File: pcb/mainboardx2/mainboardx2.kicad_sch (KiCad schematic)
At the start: 28 parts, among them J1 Compass, J10 Right, J11 Back, J12 Conn_01x03_Socket, J13 Conn_01x03_Socket, J14 Conn_01x03_Socket, J15 Conn_01x03_Socket, J16 Conn_01x03_Socket, J17 Conn_01x03_Socket, J18 Conn_01x03_Socket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

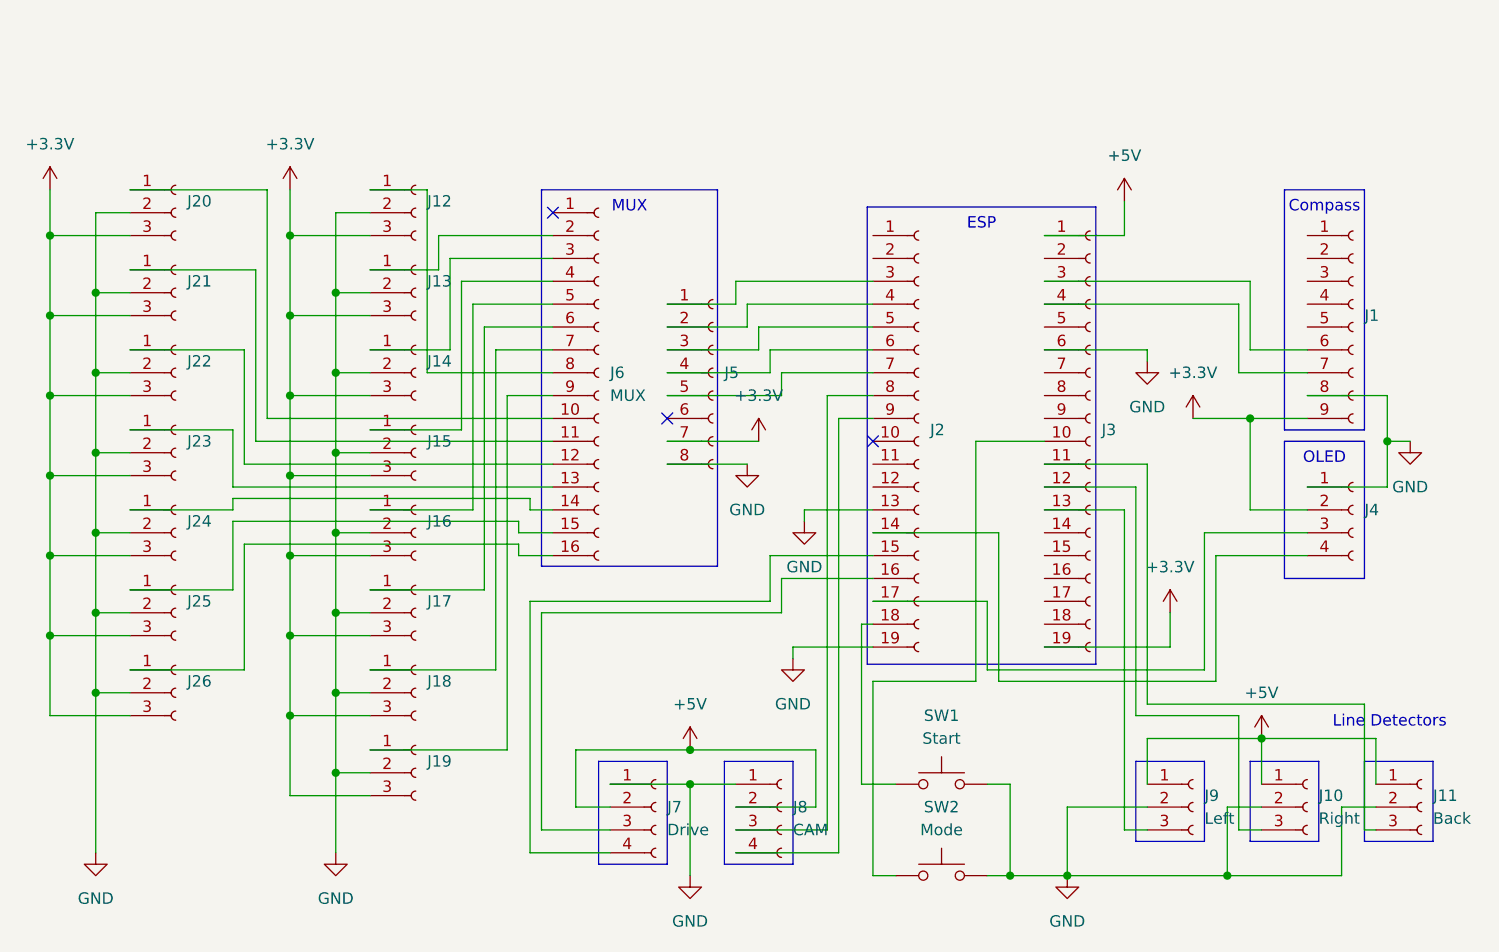
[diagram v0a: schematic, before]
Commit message: pins remapping
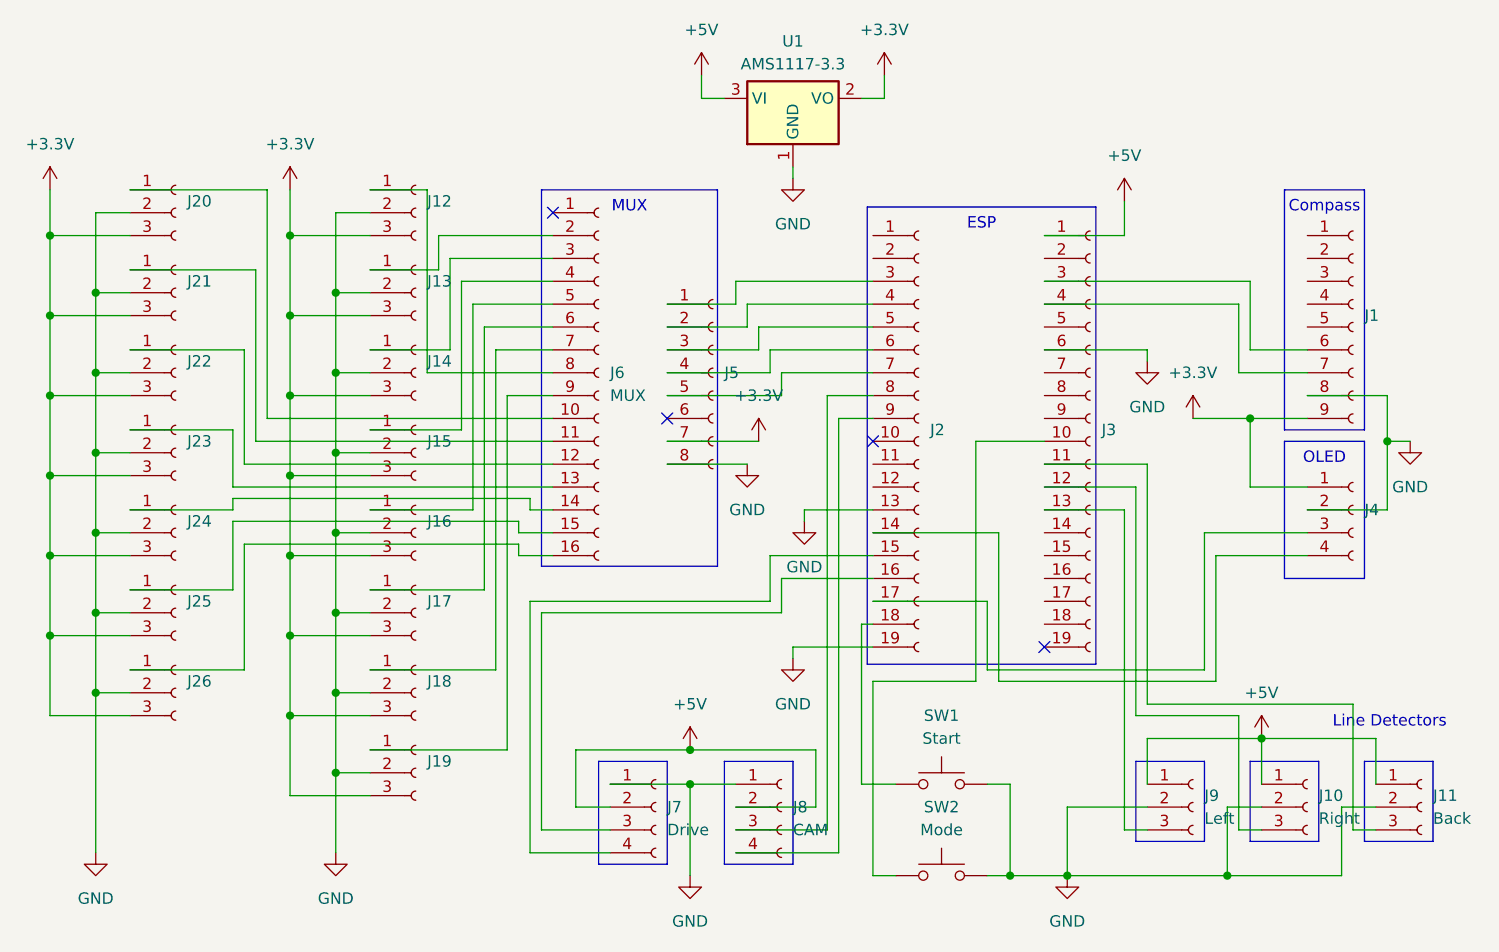
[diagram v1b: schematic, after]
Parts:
- added U1: AMS1117-3.3, Package_TO_SOT_SMD:SOT-223-3_TabPin2, symbol Regulator_Linear:AMS1117-3.3
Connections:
- net +3.3V: now also J4.1 (Pin_1), U1.2 (VO); no longer J3.19 (Pin_19), J4.2 (Pin_2)
- net +5V: now also U1.3 (VI)
- net GND: now also J4.2 (Pin_2), U1.1 (GND); no longer J4.1 (Pin_1)
- no-connect marks 3 -> 4

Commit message: calibration
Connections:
- net at J2.3 (Pin_3): no longer J5.1 (Pin_1)
- net at J3.5 (Pin_5): now also J5.1 (Pin_1)
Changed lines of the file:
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@@
 	(wire
 		(pts
-			(xy 73.66 54.61) (xy 69.85 54.61)
+			(xy 171.45 66.04) (xy 171.45 68.58)
 		)
 		(stroke
@@
 	(wire
 		(pts
-			(xy 38.1 57.15) (xy 38.1 66.04)
+			(xy 73.66 54.61) (xy 69.85 54.61)
 		)
 		(stroke
@@
 	(wire
 		(pts
-			(xy 46.99 83.82) (xy 38.1 83.82)
+			(xy 38.1 57.15) (xy 38.1 66.04)
 		)
 		(stroke
@@
 	(wire
 		(pts
-			(xy 73.66 105.41) (xy 88.9 105.41)
+			(xy 46.99 83.82) (xy 38.1 83.82)
 		)
 		(stroke
@@
 	(wire
 		(pts
-			(xy 114.3 53.34) (xy 129.54 53.34)
+			(xy 73.66 105.41) (xy 88.9 105.41)
 		)
 		(stroke
@@
 	(wire
 		(pts
+			(xy 125.73 53.34) (xy 125.73 43.18)
+		)
+		(stroke
+			(width 0)
+			(type default)
+		)
+	)
+	(wire
+		(pts
 			(xy 125.73 68.58) (xy 129.54 68.58)
 		)
@@
 	(wire
 		(pts
+			(xy 125.73 43.18) (xy 143.51 43.18)
+		)
+		(stroke
+			(width 0)
+			(type default)
+		)
+	)
+	(wire
+		(pts
 			(xy 90.17 80.01) (xy 90.17 81.28)
 		)
@@
 	(wire
 		(pts
+			(xy 114.3 53.34) (xy 125.73 53.34)
+		)
+		(stroke
+			(width 0)
+			(type default)
+		)
+	)
+	(wire
+		(pts
 			(xy 129.54 119.38) (xy 132.08 119.38)
 		)
@@
 	(wire
 		(pts
+			(xy 143.51 43.18) (xy 143.51 58.42)
+		)
+		(stroke
+			(width 0)
+			(type default)
+		)
+	)
+	(wire
+		(pts
 			(xy 73.66 66.04) (xy 64.77 66.04)
 		)
@@
 	(wire
 		(pts
-			(xy 148.59 60.96) (xy 160.02 60.96)
+			(xy 148.59 60.96) (xy 157.48 60.96)
 		)
 		(stroke
@@
 	(wire
 		(pts
-			(xy 160.02 60.96) (xy 160.02 62.23)
+			(xy 157.48 60.96) (xy 157.48 62.23)
 		)
 		(stroke
@@
 	(wire
 		(pts
-			(xy 165.1 68.58) (xy 171.45 68.58)
+			(xy 167.64 66.04) (xy 171.45 66.04)
 		)
 		(stroke
@@
 	(wire
 		(pts
+			(xy 143.51 58.42) (xy 148.59 58.42)
+		)
+		(stroke
+			(width 0)
+			(type default)
+		)
+	)
+	(wire
+		(pts
 			(xy 144.78 119.38) (xy 151.13 119.38)
 		)
@@
 	(symbol
 		(lib_id "power:+3.3V")
-		(at 165.1 68.58 0)
+		(at 167.64 66.04 0)
 		(unit 1)
 		(exclude_from_sim no)
@@
 		(fields_autoplaced yes)
 		(property "Reference" "#PWR010"
-			(at 165.1 72.39 0)
+			(at 167.64 69.85 0)
 			(effects
 				(font
@@
 		)
 		(property "Value" "+3.3V"
-			(at 165.1 63.5 0)
+			(at 167.64 60.96 0)
 			(effects
 				(font
@@
 		)
 		(property "Footprint" ""
-			(at 165.1 68.58 0)
+			(at 167.64 66.04 0)
 			(effects
 				(font
@@
 		)
 		(property "Datasheet" ""
-			(at 165.1 68.58 0)
+			(at 167.64 66.04 0)
 			(effects
 				(font
@@
 		)
 		(property "Description" "Power symbol creates a global label with name \"+3.3V\""
-			(at 165.1 68.58 0)
+			(at 167.64 66.04 0)
 			(effects
 				(font
@@
 		(on_board yes)
 		(dnp no)
-		(fields_autoplaced yes)
 		(property "Reference" "J3"
-			(at 154.94 69.8499 0)
+			(at 145.288 69.85 0)
 			(effects
 				(font
@@
 	(symbol
 		(lib_id "power:GND")
-		(at 160.02 62.23 0)
+		(at 157.48 62.23 0)
 		(unit 1)
 		(exclude_from_sim no)
@@
 		(fields_autoplaced yes)
 		(property "Reference" "#PWR02"
-			(at 160.02 68.58 0)
+			(at 157.48 68.58 0)
 			(effects
 				(font
@@
 		)
 		(property "Value" "GND"
-			(at 160.02 67.31 0)
+			(at 157.48 67.31 0)
 			(effects
 				(font
@@
 		)
 		(property "Footprint" ""
-			(at 160.02 62.23 0)
+			(at 157.48 62.23 0)
 			(effects
 				(font
@@
 		)
 		(property "Datasheet" ""
-			(at 160.02 62.23 0)
+			(at 157.48 62.23 0)
 			(effects
 				(font
@@
 		)
 		(property "Description" "Power symbol creates a global label with name \"GND\" , ground"
-			(at 160.02 62.23 0)
+			(at 157.48 62.23 0)
 			(effects
 				(font
